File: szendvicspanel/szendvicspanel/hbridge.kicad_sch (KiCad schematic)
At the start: 0 parts

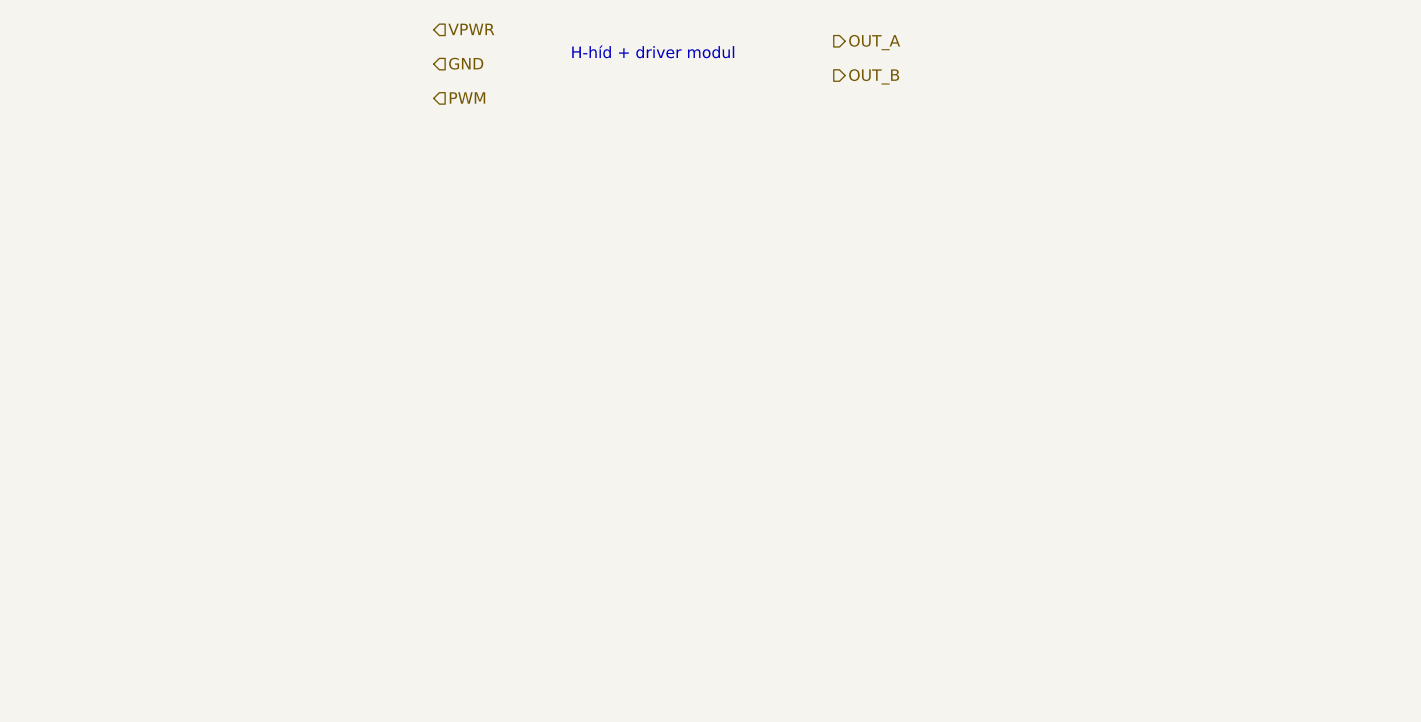
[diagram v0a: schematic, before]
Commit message: #5-ös issue, H-híd és driver modul
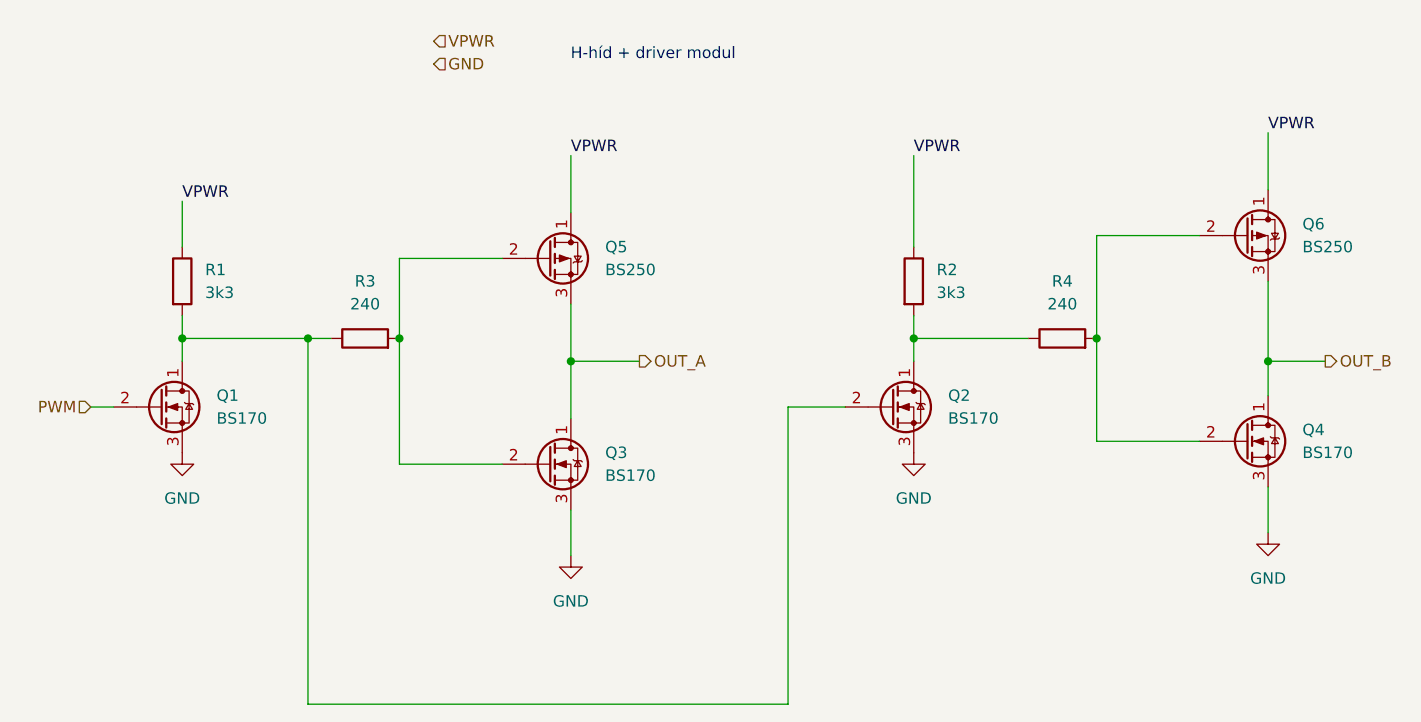
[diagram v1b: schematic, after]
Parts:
- added Q1, Q2, Q3, Q4: BS170, Package_TO_SOT_THT:TO-92_Inline, symbol Transistor_FET:BS170
- added Q5, Q6: BS250, Package_TO_SOT_THT:TO-92_Inline, symbol Transistor_FET:BS250
- added R1, R2: 3k3, symbol Device:R
- added R3, R4: 240, symbol Device:R
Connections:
- net GND: now also Q1.3 (S), Q2.3 (S), Q3.3 (S), Q4.3 (S)
- net OUT_A: now also Q3.1 (D), Q5.3 (S)
- net OUT_B: now also Q4.1 (D), Q6.3 (S)
- net PWM: now also Q1.2 (G)
- net VPWR: now also Q5.1 (D), Q6.1 (D), R1.1, R2.1
- new net: Q4.2 (G), Q6.2 (G), R4.2
- new net: Q3.2 (G), Q5.2 (G), R3.2
- new net: Q2.1 (D), R2.2, R4.1
- new net: Q1.1 (D), Q2.2 (G), R1.2, R3.1
